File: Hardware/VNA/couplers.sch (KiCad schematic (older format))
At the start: 4 parts

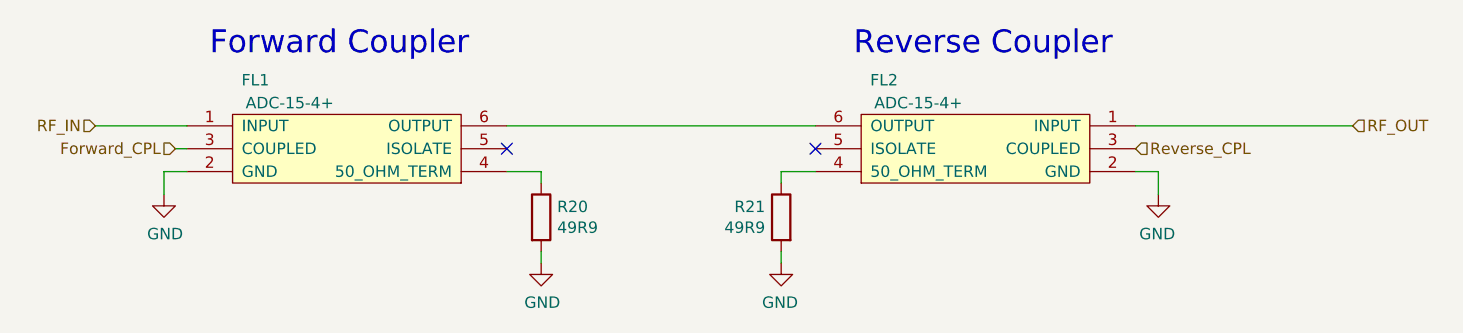
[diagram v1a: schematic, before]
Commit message: prelim schematic capture complete
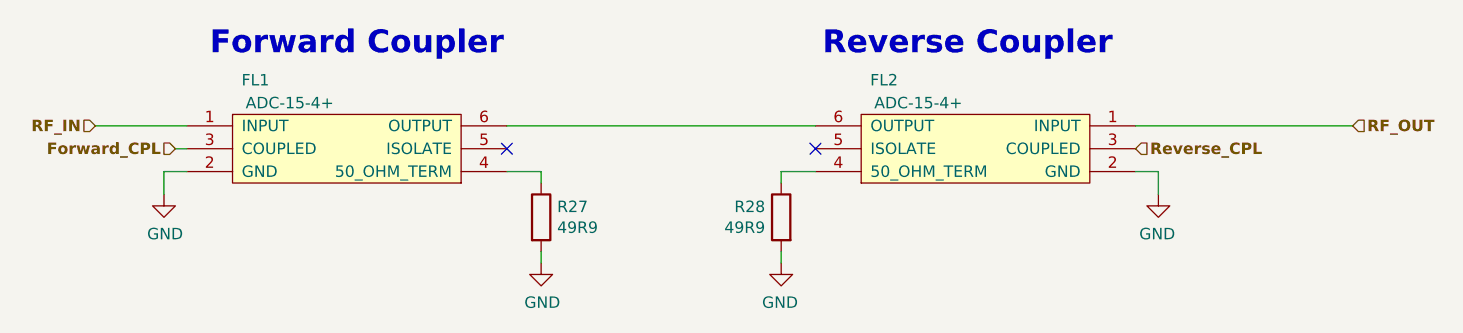
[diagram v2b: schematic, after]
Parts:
- renumbered R20 to R27, R21 to R28
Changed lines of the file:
@@
 $Descr A4 11693 8268
 encoding utf-8
-Sheet 6 8
+Sheet 5 8
 Title "Directional Couplers"
 Date "2019-04-06"
@@
 NoConn ~ 4800 2050
 $Comp
-L Device:R R20
+L Device:R R27
 U 1 1 5C294D81
 P 4950 2350
-F 0 "R20" H 5020 2396 50  0000 L CNN
+F 0 "R27" H 5020 2396 50  0000 L CNN
 F 1 "49R9" H 5020 2305 50  0000 L CNN
 F 2 "Resistor_SMD:R_0603_1608Metric" V 4880 2350 50  0001 C CNN
@@
 $EndComp
 $Comp
-L power:GND #PWR049
+L power:GND #PWR070
 U 1 1 5C294DD0
 P 4950 2550
-F 0 "#PWR049" H 4950 2300 50  0001 C CNN
+F 0 "#PWR070" H 4950 2300 50  0001 C CNN
 F 1 "GND" H 4955 2377 50  0000 C CNN
 F 2 "" H 4950 2550 50  0001 C CNN
@@
 $EndComp
 $Comp
-L power:GND #PWR048
+L power:GND #PWR069
 U 1 1 5C294DFD
 P 3300 2250
-F 0 "#PWR048" H 3300 2000 50  0001 C CNN
+F 0 "#PWR069" H 3300 2000 50  0001 C CNN
 F 1 "GND" H 3305 2077 50  0000 C CNN
 F 2 "" H 3300 2250 50  0001 C CNN
@@
 Wire Wire Line
 	3300 2150 3300 2250
-Text Notes 3500 1650 0    100  ~ 0
+Text Notes 3500 1650 0    100  ~ 6
 Forward Coupler
 $Comp
@@
 NoConn ~ 6150 2050
 $Comp
-L power:GND #PWR051
+L power:GND #PWR072
 U 1 1 5CC49779
 P 7650 2250
-F 0 "#PWR051" H 7650 2000 50  0001 C CNN
+F 0 "#PWR072" H 7650 2000 50  0001 C CNN
 F 1 "GND" H 7655 2077 50  0000 C CNN
 F 2 "" H 7650 2250 50  0001 C CNN
@@
 Wire Wire Line
 	7650 2150 7650 2250
-Text Notes 7450 1650 2    100  ~ 0
+Text Notes 7450 1650 2    100  ~ 6
 Reverse Coupler
 Wire Wire Line
@@
 	4950 2150 4950 2200
 $Comp
-L Device:R R21
+L Device:R R28
 U 1 1 5CC51D15
 P 6000 2350
-F 0 "R21" H 6070 2396 50  0000 L CNN
+F 0 "R28" H 6070 2396 50  0000 L CNN
 F 1 "49R9" H 6070 2305 50  0000 L CNN
 F 2 "Resistor_SMD:R_0603_1608Metric" V 5930 2350 50  0001 C CNN
@@
 $EndComp
 $Comp
-L power:GND #PWR050
+L power:GND #PWR071
 U 1 1 5CC51D1B
 P 6000 2550
-F 0 "#PWR050" H 6000 2300 50  0001 C CNN
+F 0 "#PWR071" H 6000 2300 50  0001 C CNN
 F 1 "GND" H 6005 2377 50  0000 C CNN
 F 2 "" H 6000 2550 50  0001 C CNN
@@
 Wire Wire Line
 	3400 2050 3350 2050
-Text HLabel 3350 2050 0    50   Input ~ 0
+Text HLabel 3350 2050 0    50   Input ~ 6
 Forward_CPL
-Text HLabel 7550 2050 2    50   Input ~ 0
+Text HLabel 7550 2050 2    50   Input ~ 6
 Reverse_CPL
-Text HLabel 3000 1950 0    50   Input ~ 0
+Text HLabel 3000 1950 0    50   Input ~ 6
 RF_IN
-Text HLabel 8500 1950 2    50   Input ~ 0
+Text HLabel 8500 1950 2    50   Input ~ 6
 RF_OUT
 $EndSCHEMATC

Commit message: all 3d models created, prelim bom generated
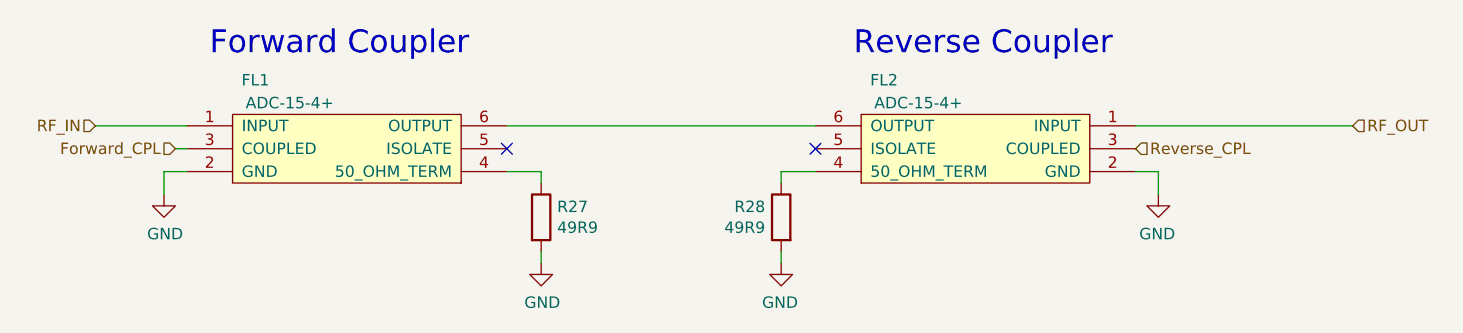
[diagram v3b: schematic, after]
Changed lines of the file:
@@
 Wire Wire Line
 	3300 2150 3300 2250
-Text Notes 3500 1650 0    100  ~ 6
+Text Notes 3500 1650 0    100  ~ 0
 Forward Coupler
 $Comp
@@
 Wire Wire Line
 	7650 2150 7650 2250
-Text Notes 7450 1650 2    100  ~ 6
+Text Notes 7450 1650 2    100  ~ 0
 Reverse Coupler
 Wire Wire Line
@@
 Wire Wire Line
 	3400 2050 3350 2050
-Text HLabel 3350 2050 0    50   Input ~ 6
+Text HLabel 3350 2050 0    50   Input ~ 0
 Forward_CPL
-Text HLabel 7550 2050 2    50   Input ~ 6
+Text HLabel 7550 2050 2    50   Input ~ 0
 Reverse_CPL
-Text HLabel 3000 1950 0    50   Input ~ 6
+Text HLabel 3000 1950 0    50   Input ~ 0
 RF_IN
-Text HLabel 8500 1950 2    50   Input ~ 6
+Text HLabel 8500 1950 2    50   Input ~ 0
 RF_OUT
 $EndSCHEMATC

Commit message: More schematic changes + updated functionals
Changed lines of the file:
@@
 Wire Wire Line
 	3300 2150 3300 2250
-Text Notes 3500 1650 0    100  ~ 0
+Text Notes 3500 1650 0    100  ~ 6
 Forward Coupler
 $Comp
@@
 Wire Wire Line
 	7650 2150 7650 2250
-Text Notes 7450 1650 2    100  ~ 0
+Text Notes 7450 1650 2    100  ~ 6
 Reverse Coupler
 Wire Wire Line
@@
 Wire Wire Line
 	3400 2050 3350 2050
-Text HLabel 3350 2050 0    50   Input ~ 0
+Text HLabel 3350 2050 0    50   Input ~ 6
 Forward_CPL
-Text HLabel 7550 2050 2    50   Input ~ 0
+Text HLabel 7550 2050 2    50   Input ~ 6
 Reverse_CPL
-Text HLabel 3000 1950 0    50   Input ~ 0
+Text HLabel 3000 1950 0    50   Input ~ 6
 RF_IN
-Text HLabel 8500 1950 2    50   Input ~ 0
+Text HLabel 8500 1950 2    50   Input ~ 6
 RF_OUT
 $EndSCHEMATC

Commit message: first day of layout / routing done
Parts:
- renumbered FL1 to HY1, FL2 to HY2
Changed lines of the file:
@@
 $EndDescr
 $Comp
-L VNA_Symbols:ADC-15-4+ FL1
+L VNA_Symbols:ADC-15-4+ HY1
 U 1 1 5C294AFE
 P 4050 1900
-F 0 "FL1" H 3700 2050 50  0000 C CNN
+F 0 "HY1" H 3700 2050 50  0000 C CNN
 F 1 "ADC-15-4+" H 3850 1950 50  0000 C CNN
 F 2 "VNA_Footprints:CD542" H 4050 1900 50  0001 C CNN
@@
 Wire Wire Line
 	3300 2150 3300 2250
-Text Notes 3500 1650 0    100  ~ 6
+Text Notes 3500 1650 0    100  ~ 20
 Forward Coupler
 $Comp
-L VNA_Symbols:ADC-15-4+ FL2
+L VNA_Symbols:ADC-15-4+ HY2
 U 1 1 5CC49764
 P 6900 1900
-F 0 "FL2" H 7350 2050 50  0000 C CNN
+F 0 "HY2" H 7350 2050 50  0000 C CNN
 F 1 "ADC-15-4+" H 7200 1950 50  0000 C CNN
 F 2 "VNA_Footprints:CD542" H 6900 1900 50  0001 C CNN
@@
 Wire Wire Line
 	7650 2150 7650 2250
-Text Notes 7450 1650 2    100  ~ 6
+Text Notes 7450 1650 2    100  ~ 20
 Reverse Coupler
 Wire Wire Line
@@
 Wire Wire Line
 	3400 2050 3350 2050
-Text HLabel 3350 2050 0    50   Input ~ 6
+Text HLabel 3350 2050 0    50   Input ~ 10
 Forward_CPL
-Text HLabel 7550 2050 2    50   Input ~ 6
+Text HLabel 7550 2050 2    50   Input ~ 10
 Reverse_CPL
-Text HLabel 3000 1950 0    50   Input ~ 6
+Text HLabel 3000 1950 0    50   Input ~ 10
 RF_IN
-Text HLabel 8500 1950 2    50   Input ~ 6
+Text HLabel 8500 1950 2    50   Input ~ 10
 RF_OUT
 $EndSCHEMATC

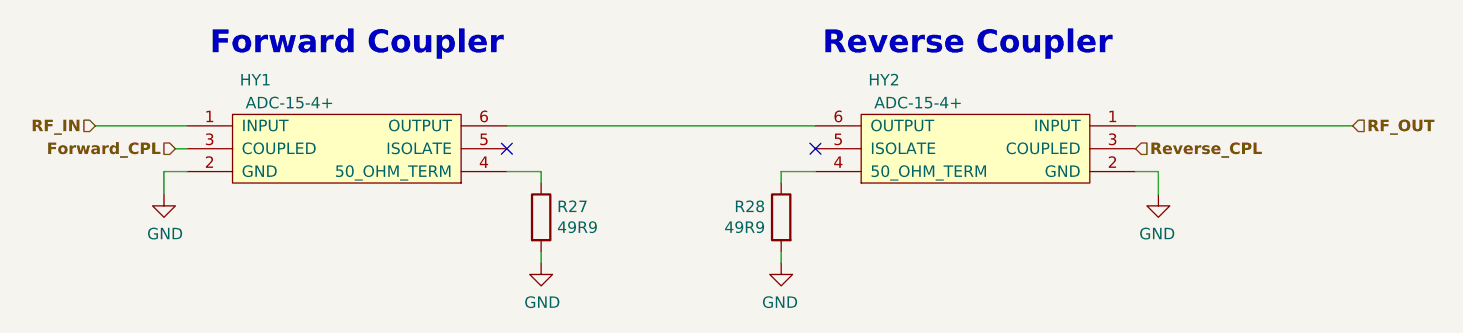
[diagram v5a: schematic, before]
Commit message: fix KiCad 5.1.0 bold after plot issue on schematics
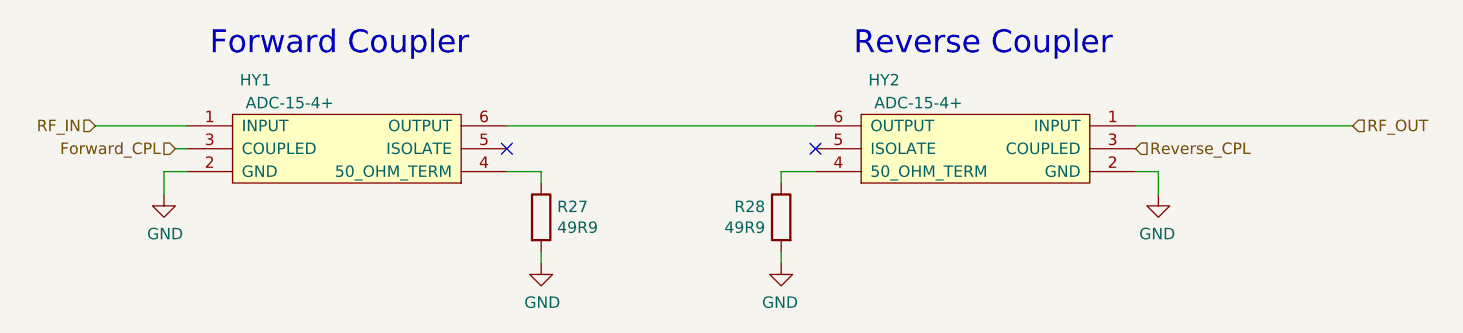
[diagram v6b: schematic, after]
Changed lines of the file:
@@
 Wire Wire Line
 	3300 2150 3300 2250
-Text Notes 3500 1650 0    100  ~ 20
+Text Notes 3500 1650 0    100  ~ 0
 Forward Coupler
 $Comp
@@
 Wire Wire Line
 	7650 2150 7650 2250
-Text Notes 7450 1650 2    100  ~ 20
+Text Notes 7450 1650 2    100  ~ 0
 Reverse Coupler
 Wire Wire Line
@@
 Wire Wire Line
 	3400 2050 3350 2050
-Text HLabel 3350 2050 0    50   Input ~ 10
+Text HLabel 3350 2050 0    50   Input ~ 0
 Forward_CPL
-Text HLabel 7550 2050 2    50   Input ~ 10
+Text HLabel 7550 2050 2    50   Input ~ 0
 Reverse_CPL
-Text HLabel 3000 1950 0    50   Input ~ 10
+Text HLabel 3000 1950 0    50   Input ~ 0
 RF_IN
-Text HLabel 8500 1950 2    50   Input ~ 10
+Text HLabel 8500 1950 2    50   Input ~ 0
 RF_OUT
 $EndSCHEMATC
